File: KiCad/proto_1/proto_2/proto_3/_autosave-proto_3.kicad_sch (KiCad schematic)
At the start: 11 parts, among them J2 Conn_2Rows-07Pins

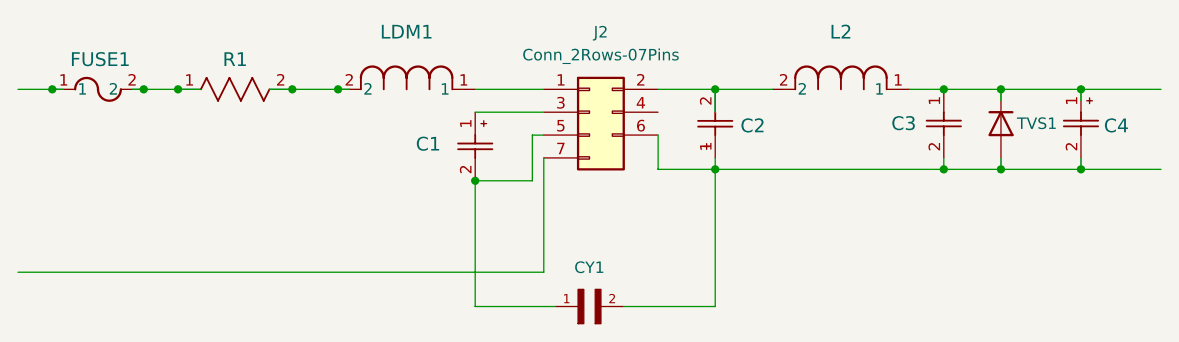
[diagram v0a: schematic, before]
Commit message: changing symbols and footprints
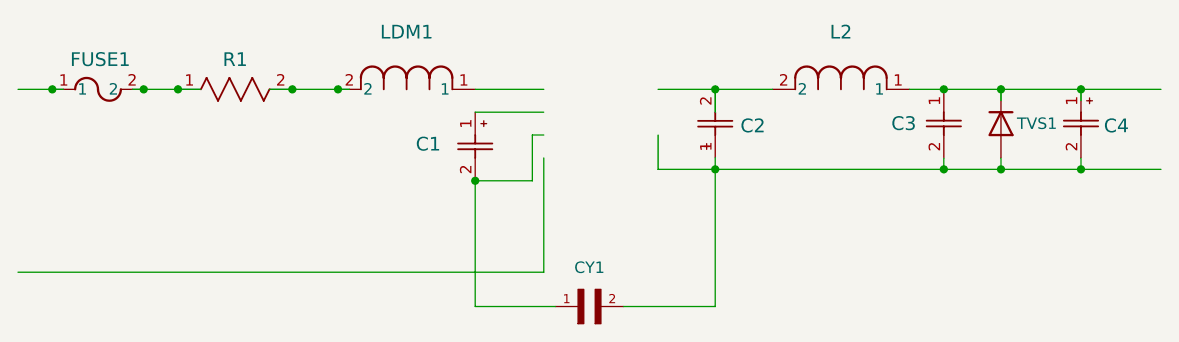
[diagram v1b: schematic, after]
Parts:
- removed J2: Conn_2Rows-07Pins, symbol Connector_Generic:Conn_2Rows-07Pins
- C3: footprint CAP_6.3X11_RUB -> Capacitor-100uF-35V:CAP_6.3X11_RUB
- C4: footprint CAP_UEP_5X11_NCH -> Capacitor-,1uF-50V:CAP_UEP_5X11_NCH
- L2, LDM1: footprint IND_BOURNS_RLB9012 -> Inductor-4.7uH-60ohm:IND_BOURNS_RLB9012
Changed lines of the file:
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@@
 			)
 		)
-		(property "Footprint" "IND_BOURNS_RLB9012"
+		(property "Footprint" "Inductor-4.7uH-60ohm:IND_BOURNS_RLB9012"
 			(at 58.42 40.64 0)
 			(effects
@@
 			)
 		)
-		(property "Footprint" "CAP_UEP_5X11_NCH"
+		(property "Footprint" "Capacitor-,1uF-50V:CAP_UEP_5X11_NCH"
 			(at 140.97 40.64 0)
 			(effects
@@
 			)
 		)
-		(property "Footprint" "IND_BOURNS_RLB9012"
+		(property "Footprint" "Inductor-4.7uH-60ohm:IND_BOURNS_RLB9012"
 			(at 106.68 40.64 0)
 			(effects
@@
 			)
 		)
-		(property "Footprint" "CAP_6.3X11_RUB"
+		(property "Footprint" "Capacitor-100uF-35V:CAP_6.3X11_RUB"
 			(at 125.73 40.64 0)
 			(effects
@@
 					(unit 1)
 				)
-			)
-		)
-	)
-	(symbol
-		(lib_id "Connector_Generic:Conn_2Rows-07Pins")
-		(at 86.36 43.18 0)
-		(unit 1)
-		(exclude_from_sim no)
-		(in_bom yes)
-		(on_board yes)
-		(dnp no)
-		(fields_autoplaced yes)
-		(property "Reference" "J2"
-			(at 87.63 34.29 0)
-			(effects
-				(font
-					(size 1.27 1.27)
-				)
-			)
-		)
-		(property "Value" "Conn_2Rows-07Pins"
-			(at 87.63 36.83 0)
-			(effects
-				(font
-					(size 1.27 1.27)
-				)
-			)
-		)
-		(property "Footprint" ""
-			(at 86.36 43.18 0)
-			(effects
-				(font
-					(size 1.27 1.27)
-				)
-				(hide yes)
-			)
-		)
-		(property "Datasheet" "~"
-			(at 86.36 43.18 0)
-			(effects
-				(font
-					(size 1.27 1.27)
-				)
-				(hide yes)
-			)
-		)
-		(property "Description" "Generic connector, double row, 07 pins, odd/even pin numbering scheme (row 1 odd numbers, row 2 even numbers), script generated (kicad-library-utils/schlib/autogen/connector/)"
-			(at 86.36 43.18 0)
-			(effects
-				(font
-					(size 1.27 1.27)
-				)
-				(hide yes)
-			)
-		)
-		(pin "4"
-		)
-		(pin "2"
-		)
-		(pin "6"
-		)
-		(pin "7"
-		)
-		(pin "3"
-		)
-		(pin "5"
-		)
-		(pin "1"
-		)
-		(instances
-			(project ""
-				(path "/3ba3c426-0aff-4728-abf4-4c9cd318aec8"
-					(reference "J2")
-					(unit 1)
-				)
